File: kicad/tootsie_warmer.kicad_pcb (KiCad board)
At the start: 2 copper layers, 3 parts, among them U1 WeMos_D1_mini

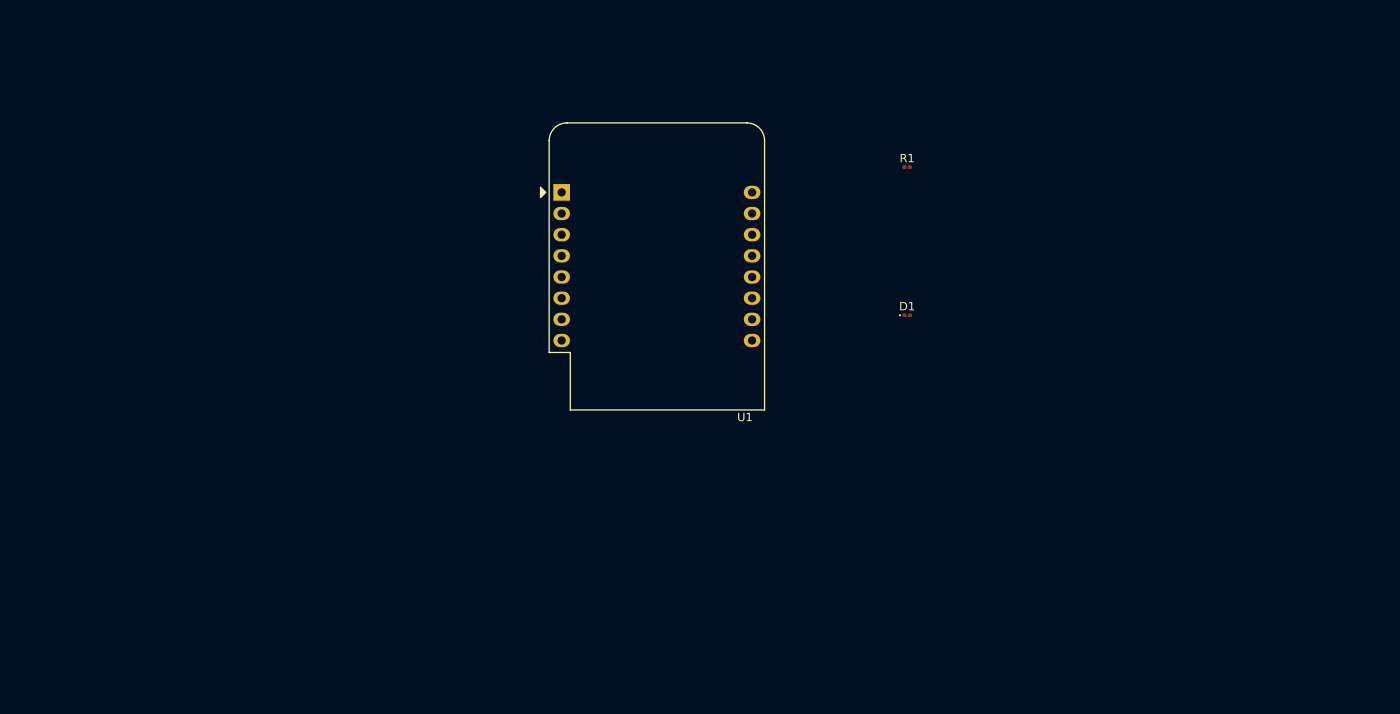
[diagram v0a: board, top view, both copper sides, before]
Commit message: Update schema to have connector for relay
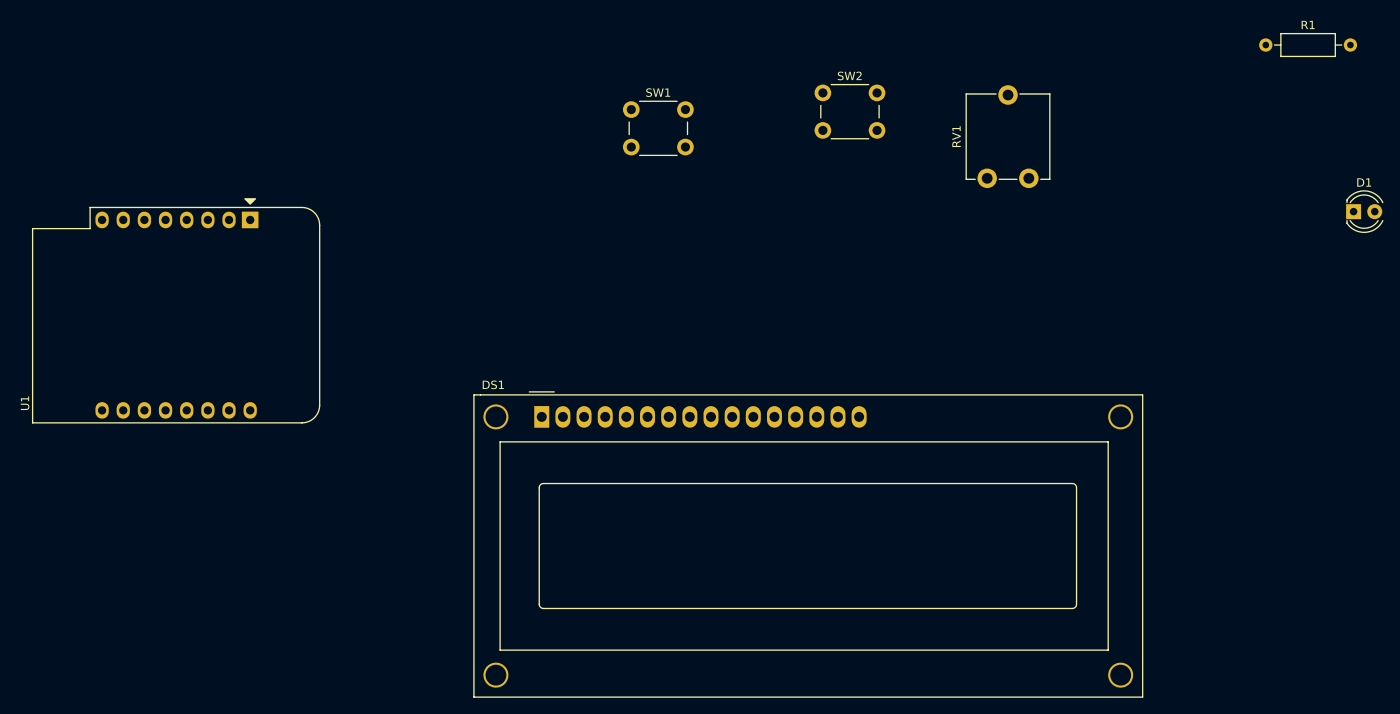
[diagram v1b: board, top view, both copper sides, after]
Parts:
- added DS1: WC1602A, Display:WC1602A, F.Cu at (106.0, 103.6)
- added RV1: R_Potentiometer, Potentiometer_THT:Potentiometer_ACP_CA9-V10_Vertical, F.Cu at (164.5, 75.0)
- added SW1: SW_Add, Button_Switch_THT:SW_PUSH_6mm_H4.3mm, F.Cu at (116.8, 66.8)
- added SW2: SW_Stop, Button_Switch_THT:SW_PUSH_6mm_H4.3mm, F.Cu at (139.8, 64.8)
- D1: footprint LED_SMD:LED_0201_0603Metric -> LED_THT:LED_D4.0mm
- R1: value R -> 220; footprint Resistor_SMD:R_0201_0603Metric -> Resistor_THT:R_Axial_DIN0207_L6.3mm_D2.5mm_P10.16mm_Horizontal
- moved D1 55.0 mm to (203.5, 79.0)
- moved R1 45.5 mm to (192.9, 59.0)
- moved U1 37.5 mm to (71.0, 80.0), turned to -90 degrees
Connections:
- U1 pad 12: unconnected-(U1-Pad12) -> Net-(SW1-Pad2)
- U1 pad 13: unconnected-(U1-Pad13) -> Net-(SW2-Pad2)
- U1 pad 14: unconnected-(U1-Pad14) -> Net-(DS1-Pad4)
- U1 pad 3: unconnected-(U1-Pad3) -> Net-(DS1-Pad11)
- U1 pad 4: unconnected-(U1-Pad4) -> Net-(DS1-Pad14)
- U1 pad 5: unconnected-(U1-Pad5) -> Net-(DS1-Pad13)
- U1 pad 6: unconnected-(U1-Pad6) -> Net-(DS1-Pad12)
- U1 pad 7: unconnected-(U1-Pad7) -> Net-(DS1-Pad6)
- U1 pad 9: unconnected-(U1-Pad9) -> Net-(U1-Pad9)
